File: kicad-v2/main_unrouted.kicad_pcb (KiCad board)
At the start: 2 copper layers, 116.8 x 71.1 mm, 26 parts, among them J3 Ext, J4 UART, J5 uSD, J6 PCM5102A, SW1 Up, SW2 Down, SW3 Left, SW4 Right, SW5 A, SW6 B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

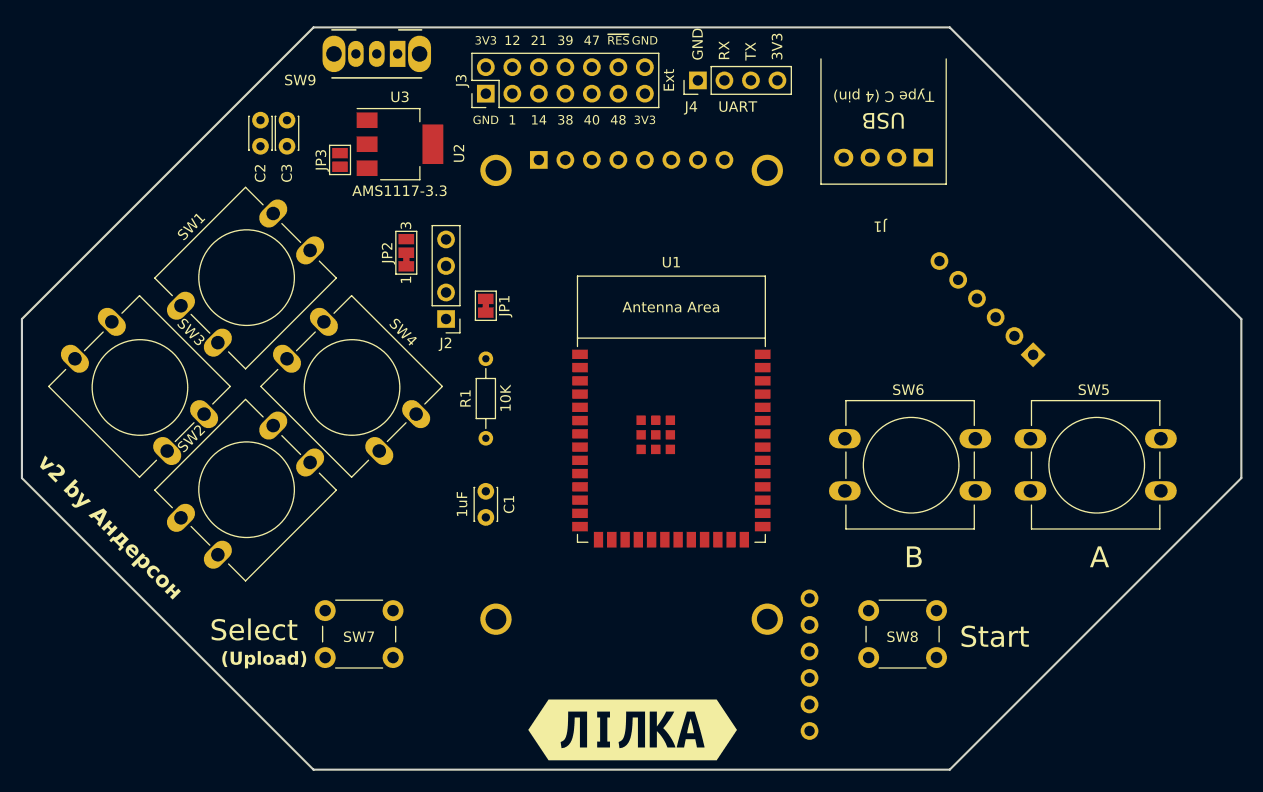
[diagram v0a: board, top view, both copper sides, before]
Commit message: kicad-v2: add MAX98357A slot
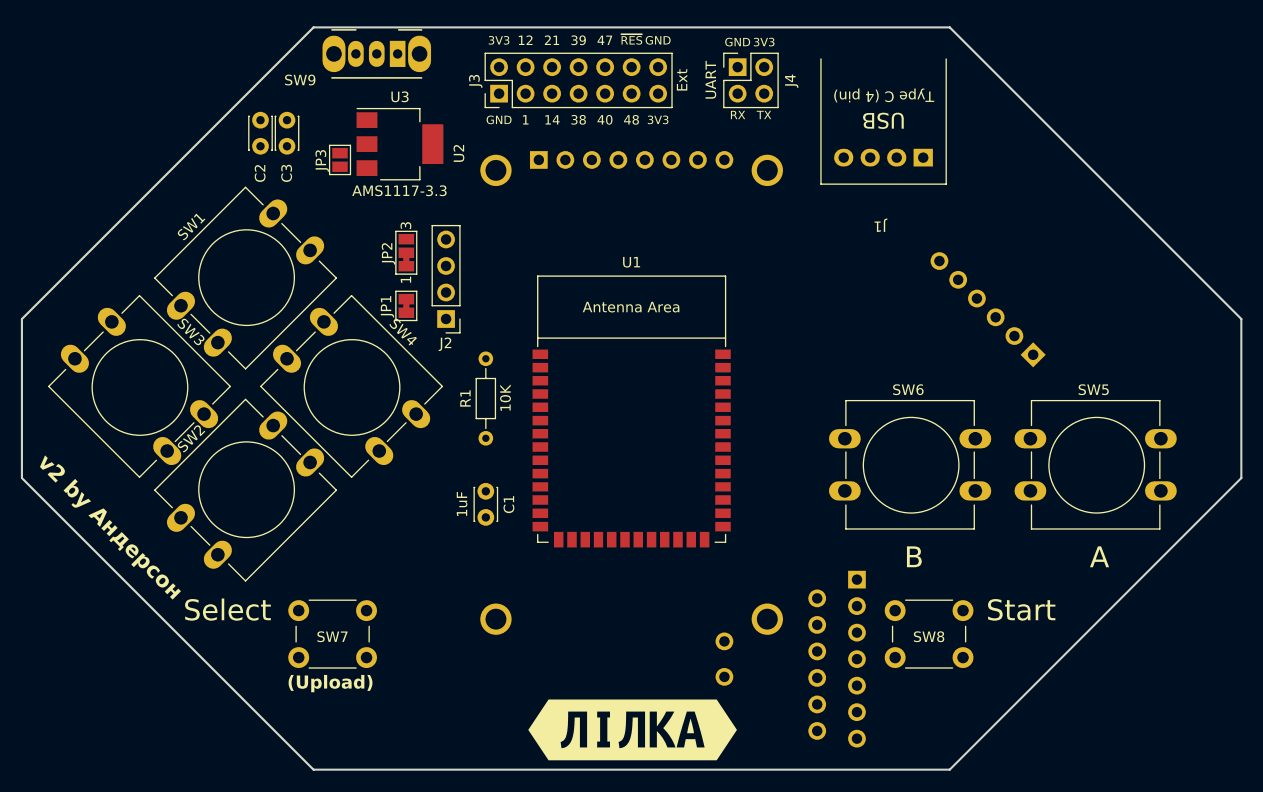
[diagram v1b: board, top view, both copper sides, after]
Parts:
- added J7: ~, footprints:MAX98357-I2S-Module, B.Cu at (110.5, 100.5)
- J4: footprint Connector_PinHeader_2.54mm:PinHeader_1x04_P2.54mm_Vertical -> Connector_PinHeader_2.54mm:PinHeader_2x02_P2.54mm_Vertical
- U1: footprint PCM_Espressif:ESP32-S3-WROOM-1 -> PCM_Espressif:ESP32-S3-WROOM-1_nognd
- moved JP1 7.62 mm to (74.9, 67.3)
- moved J4 4.02 mm to (106.7, 44.5), turned to 0 degrees
- moved U1 3.81 mm to (96.5, 80.2)
- moved SW7 2.54 mm to (64.6, 96.5)
- moved SW8 2.54 mm to (121.8, 96.5)
- moved J3 1.27 mm to (83.8, 47.0)
- moved J6 0.73 mm to (115.6, 93.4)
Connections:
- J3 pad 10: GPIO47 -> GPIO16
- J3 pad 11: GPIO48 -> GPIO17
- J3 pad 4: GPIO12/ADC2_CH0 -> GPIO8
- J3 pad 5: GPIO14 -> GPIO9
- J3 pad 6: GPIO21 -> GPIO10
- J3 pad 7: GPIO38 -> GPIO11/ADC2_CH0
- J3 pad 8: GPIO39 -> GPIO12
- J3 pad 9: GPIO40 -> GPIO15
- J4 pad 2: RX -> +3V3
- J4 pad 3: TX -> RX
- J4 pad 4: +3V3 -> TX
- U1 pad 10: MISO -> GPIO17
- U1 pad 11: DISP_D/C -> SELECT
- U1 pad 12: ~{DISP_CS} -> GPIO8
- U1 pad 17: BCK -> GPIO9
- U1 pad 18: DIN -> GPIO10
- U1 pad 19: GPIO12/ADC2_CH0 -> GPIO11/ADC2_CH0
- U1 pad 20: LRCK -> GPIO12
- U1 pad 21: SELECT -> B
- U1 pad 22: GPIO14 -> A
- U1 pad 23: GPIO21 -> BCK
- U1 pad 24: GPIO47 -> DIN
- U1 pad 25: GPIO48 -> LRCK
- U1 pad 31: GPIO38 -> ~{DISP_CS}
- U1 pad 32: GPIO39 -> DISP_D/C
- U1 pad 33: GPIO40 -> MISO
- U1 pad 34: ~{SD_CS} -> MOSI
- U1 pad 35: B -> SCK
- U1 pad 38: A -> ~{SD_CS}
- U1 pad 8: SCK -> GPIO15
- U1 pad 9: MOSI -> GPIO16
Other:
- board text added: "MAX98357A"
- board text added: "PCM5102A"
- board text added: "RX"
- board text added: "TX"

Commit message: kicad-v2: improve PCB button & uSD routing (via count = 18: manual routing for buttons & SD card)
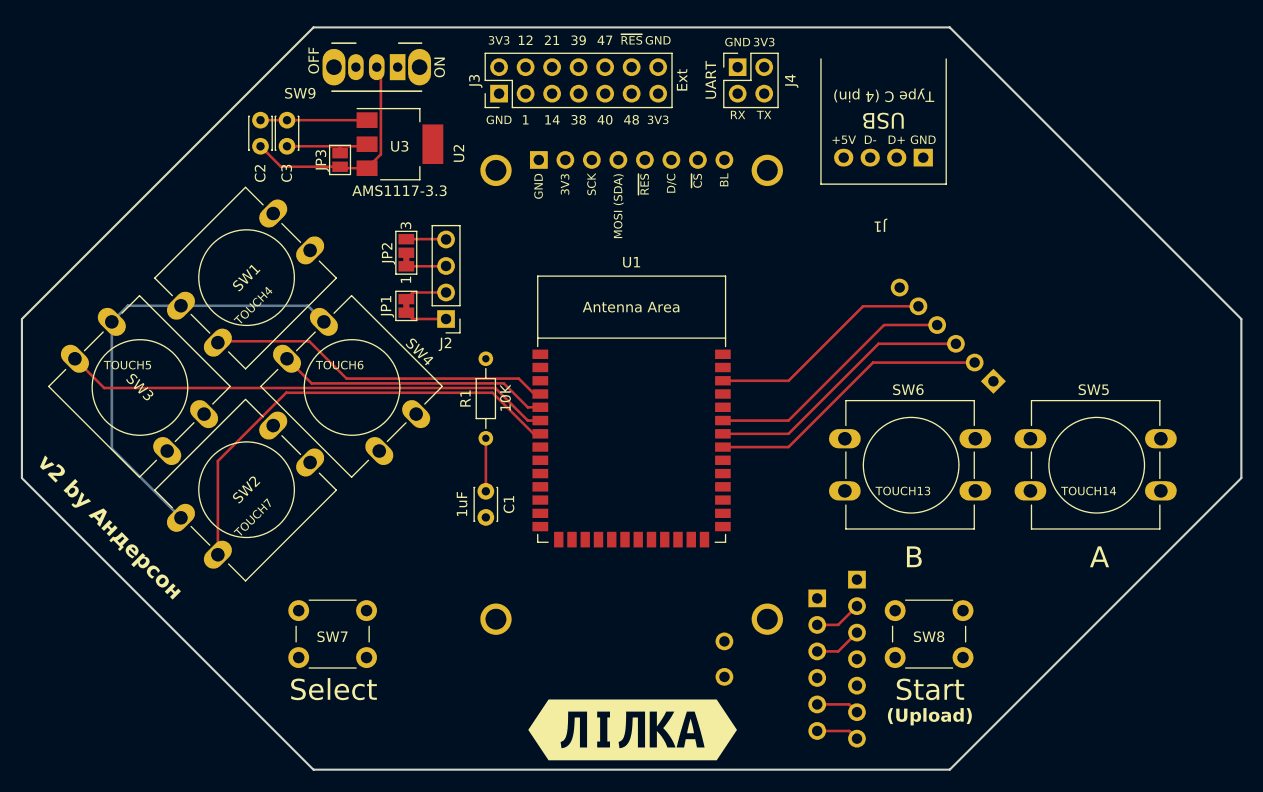
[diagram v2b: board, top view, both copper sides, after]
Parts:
- moved J5 4.58 mm to (132.1, 77.2)
- moved SW9 1.27 mm to (74.1, 44.5)
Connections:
- U1 pad 33: MISO -> ~{SD_CS}
- U1 pad 38: ~{SD_CS} -> MISO
- U1 pad 5: LEFT -> RIGHT
- U1 pad 6: RIGHT -> LEFT
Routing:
- net GND: track 0.00 -> 61.5 mm
- net LEFT: track 0.00 -> 47.0 mm
- net DOWN: track 0.00 -> 44.2 mm
- net UP: track 0.00 -> 33.0 mm
- net ~{SD_CS}: track 0.00 -> 27.5 mm
- net RIGHT: track 0.00 -> 26.2 mm
- net MOSI: track 0.00 -> 25.9 mm
- net SCK: track 0.00 -> 24.3 mm
- net MISO: track 0.00 -> 21.7 mm
- net VCC: track 0.00 -> 21.5 mm
- net +3V3: track 0.00 -> 12.5 mm
- net ~{RESET}: track 0.00 -> 5.08 mm
- net DIN: track 0.00 -> 4.56 mm
- net BCK: track 0.00 -> 4.56 mm
- net GND1: track 0.00 -> 4.07 mm
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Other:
- board text added: "+5V"
- board text added: "BL"
- board text added: "D+"
- board text added: "D-"
- board text added: "D/C"
- board text added: "MOSI (SDA)"
- board text added: "OFF"
- board text added: "ON"
- board text added: "SCK"
- board text added: "TOUCH13"
- board text added: "TOUCH14"
- board text added: "TOUCH4"
- board text added: "TOUCH5"
- board text added: "TOUCH6"
- board text added: "TOUCH7"
- board text added: "~{CS}"

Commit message: kicad-v2: cleanup buttons
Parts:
- moved SW2 13.5 mm to (65.8, 82.3), turned to -135 degrees
- moved SW3 13.5 mm to (52.0, 81.2), turned to 135 degrees
- moved SW4 13.5 mm to (72.3, 81.2), turned to 135 degrees
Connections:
- U1 pad 5: RIGHT -> LEFT
- U1 pad 6: LEFT -> RIGHT
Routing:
- net +3V3: track 12.5 -> 193.8 mm
- net GND: track 61.5 -> 235.7 mm
- net GPIO10: track 0.00 -> 126.6 mm
- net GPIO12: track 0.00 -> 117.5 mm
- net ~{DISP_CS}: track 0.00 -> 66.8 mm
- net GPIO1/ADC1_CH0: track 0.00 -> 61.2 mm, vias 0 -> 1
- net GPIO9: track 0.00 -> 56.1 mm, vias 0 -> 1
- net GPIO11/ADC2_CH0: track 0.00 -> 55.1 mm, vias 0 -> 1
- net USB+: track 0.00 -> 54.9 mm, vias 0 -> 1
- net GND1: track 4.07 -> 57.9 mm, vias 0 -> 1
- net USB-: track 0.00 -> 52.9 mm, vias 0 -> 1
- net ~{RESET}: track 5.08 -> 57.8 mm, vias 0 -> 1
- net GPIO8: track 0.00 -> 52.2 mm, vias 0 -> 1
- net GPIO16: track 0.00 -> 47.3 mm, vias 0 -> 1
- net LEFT: track 47.0 -> 0.00 mm
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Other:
- board text added: "10"
- board text added: "11"
- board text added: "15"
- board text added: "16"
- board text added: "17"
- board text added: "8"
- board text added: "9"
- board text removed: "14"
- board text removed: "21"
- board text removed: "38"
- board text removed: "39"
- board text removed: "40"
- board text removed: "47"
- board text removed: "48"
